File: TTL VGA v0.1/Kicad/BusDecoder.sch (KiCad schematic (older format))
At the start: 12 parts, among them U15 74LS74, U16 74LS32, U17 74LS10, U18 74LS32, U8 74LS139

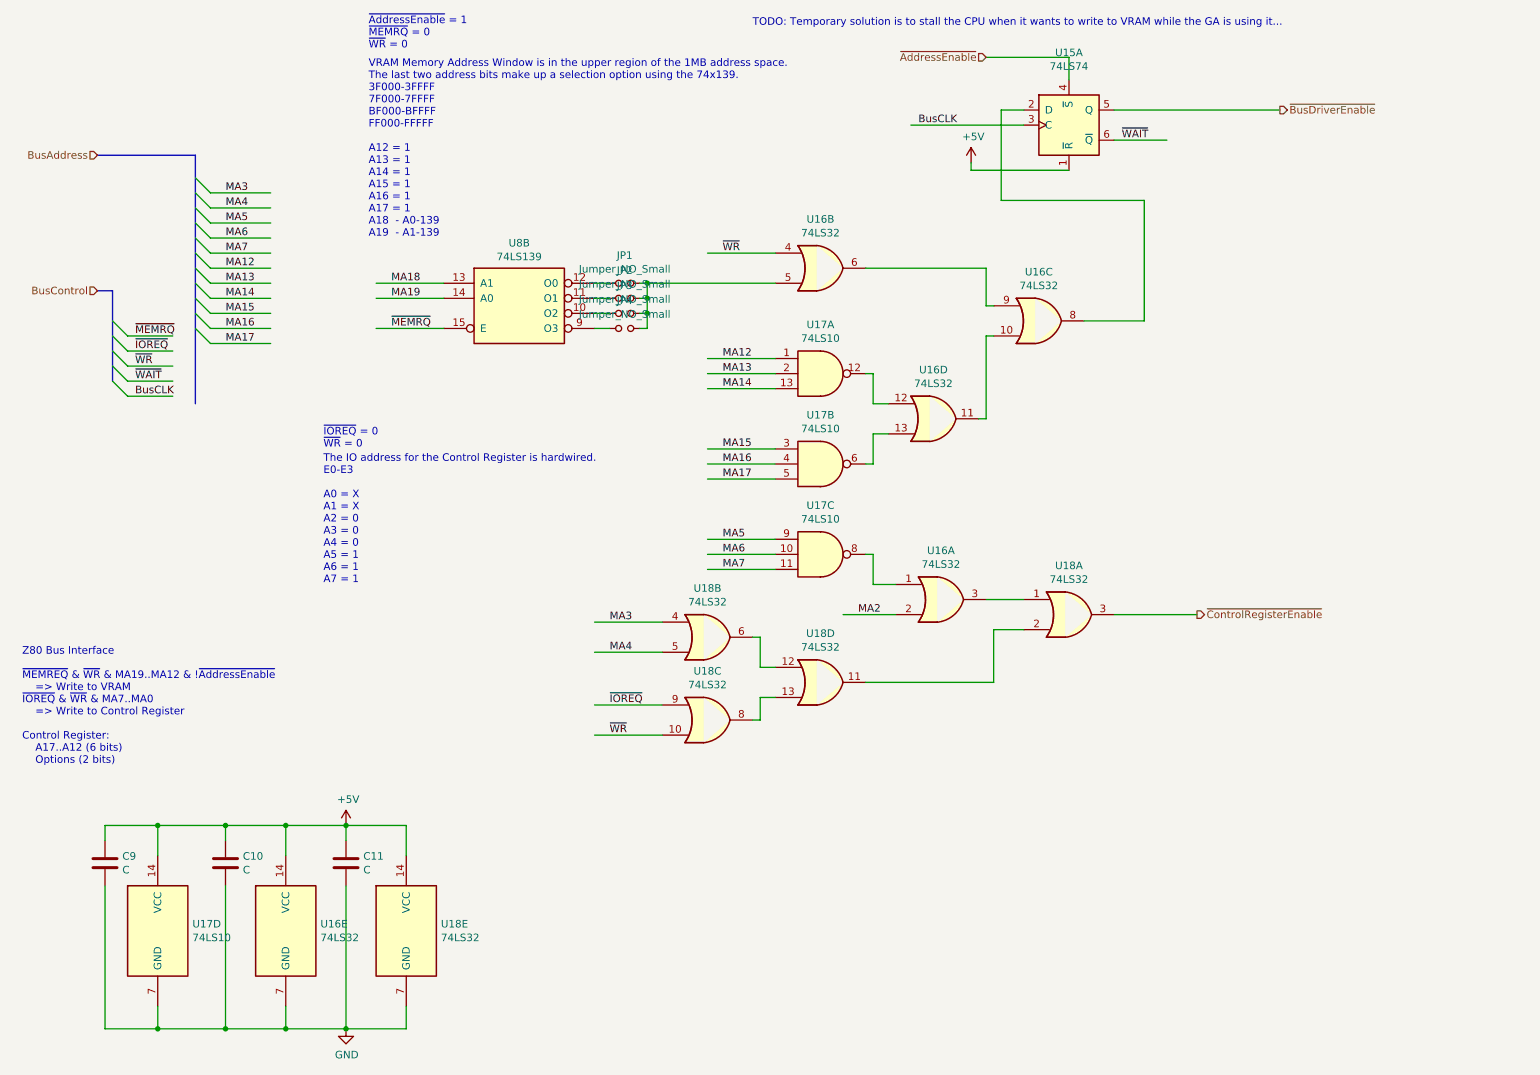
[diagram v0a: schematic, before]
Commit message: vga memory interface
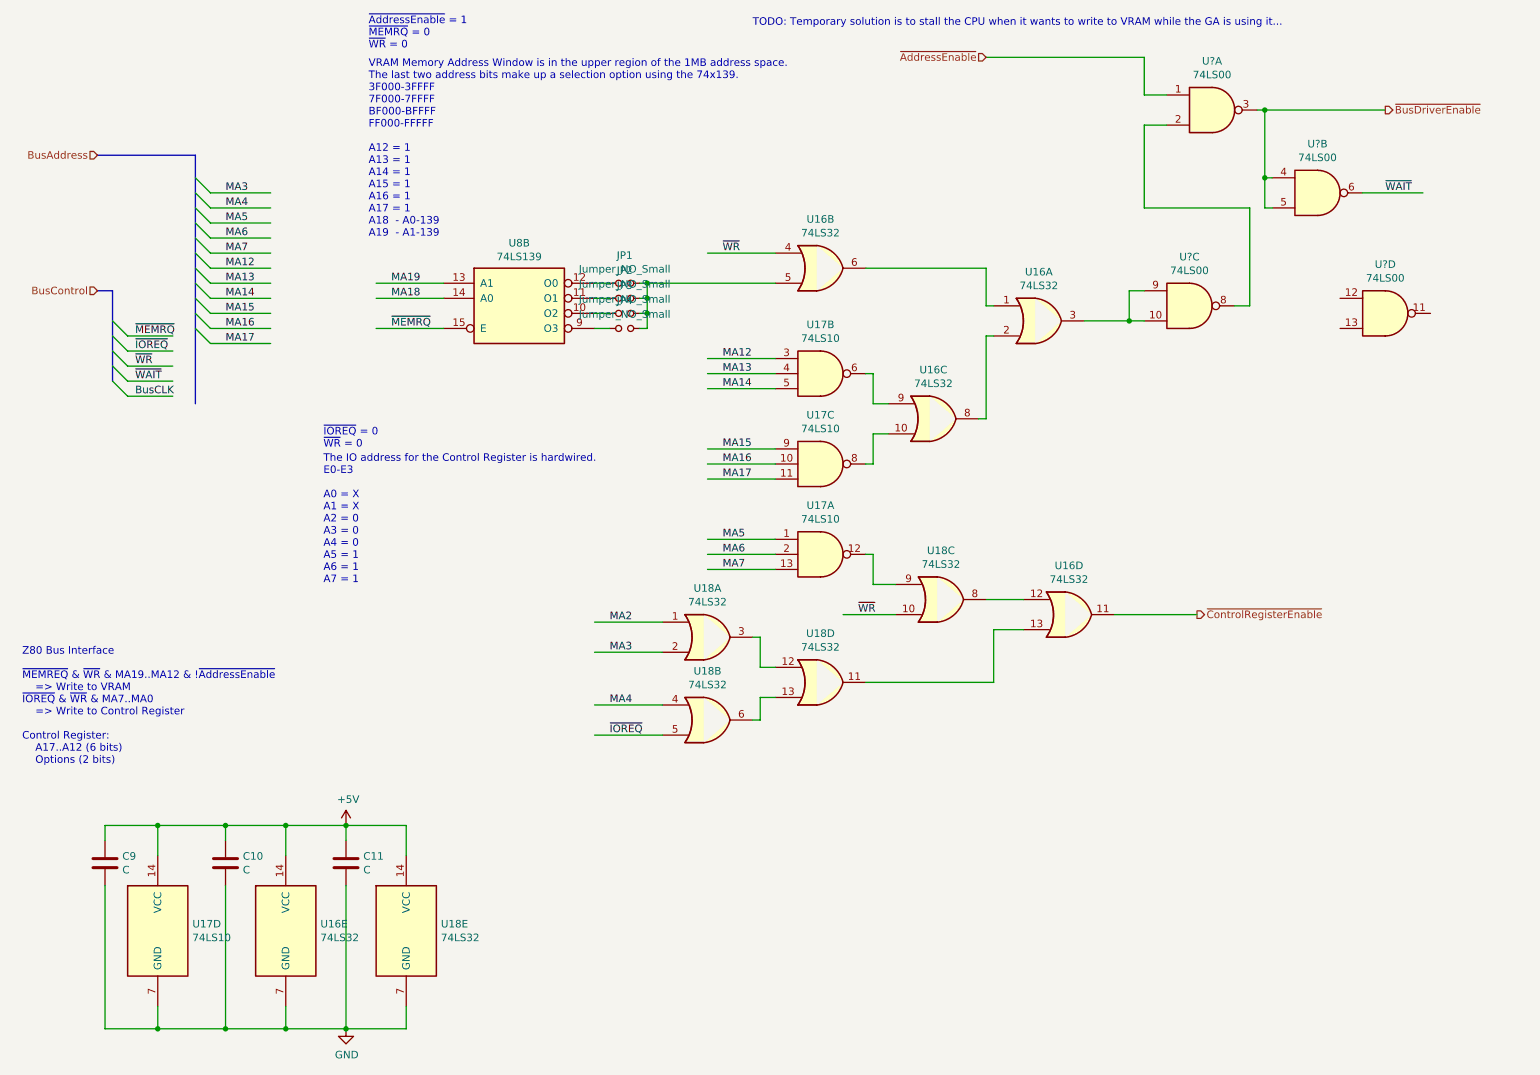
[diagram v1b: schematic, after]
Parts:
- removed U15: 74LS74, symbol 74xx:74LS74
- added U? (x4): 74LS00, symbol 74xx:74LS00
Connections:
- wire segments 106 -> 113
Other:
- moved on the sheet: U16A, U16C, U16D, U17A, U17B, U17C, U18A, U18B, U18C
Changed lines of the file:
@@
 Text HLabel 8650 4550 2    50   Output ~ 0
 ~ControlRegisterEnable
-Text HLabel 9200 1200 2    50   Output ~ 0
+Text HLabel 9900 1200 2    50   Output ~ 0
 ~BusDriverEnable
 Text HLabel 7250 850  0    50   Input ~ 0
@@
 L 74xx:74LS10 U17
 U 1 1 5E729378
+P 6150 4150
+F 0 "U17" H 6150 4475 50  0000 C CNN
+F 1 "74LS10" H 6150 4384 50  0000 C CNN
+F 2 "" H 6150 4150 50  0001 C CNN
+F 3 "http://www.ti.com/lit/gpn/sn74LS10" H 6150 4150 50  0001 C CNN
+	1    6150 4150
+	1    0    0    -1
+$EndComp
+$Comp
+L 74xx:74LS10 U17
+U 2 1 5E7295F8
 P 6150 2950
 F 0 "U17" H 6150 3275 50  0000 C CNN
@@
 F 2 "" H 6150 2950 50  0001 C CNN
 F 3 "http://www.ti.com/lit/gpn/sn74LS10" H 6150 2950 50  0001 C CNN
-	1    6150 2950
+	2    6150 2950
 	1    0    0    -1
 $EndComp
 $Comp
 L 74xx:74LS10 U17
-U 2 1 5E7295F8
+U 3 1 5E72A784
 P 6150 3550
 F 0 "U17" H 6150 3875 50  0000 C CNN
@@
 F 2 "" H 6150 3550 50  0001 C CNN
 F 3 "http://www.ti.com/lit/gpn/sn74LS10" H 6150 3550 50  0001 C CNN
-	2    6150 3550
-	1    0    0    -1
-$EndComp
-$Comp
-L 74xx:74LS10 U17
-U 3 1 5E72A784
-P 6150 4150
-F 0 "U17" H 6150 4475 50  0000 C CNN
-F 1 "74LS10" H 6150 4384 50  0000 C CNN
-F 2 "" H 6150 4150 50  0001 C CNN
-F 3 "http://www.ti.com/lit/gpn/sn74LS10" H 6150 4150 50  0001 C CNN
-	3    6150 4150
+	3    6150 3550
 	1    0    0    -1
 $EndComp
@@
 L 74xx:74LS32 U16
 U 1 1 5E72DE74
-P 6950 4450
-F 0 "U16" H 6950 4775 50  0000 C CNN
-F 1 "74LS32" H 6950 4684 50  0000 C CNN
-F 2 "" H 6950 4450 50  0001 C CNN
-F 3 "http://www.ti.com/lit/gpn/sn74LS32" H 6950 4450 50  0001 C CNN
-	1    6950 4450
+P 7600 2600
+F 0 "U16" H 7600 2925 50  0000 C CNN
+F 1 "74LS32" H 7600 2834 50  0000 C CNN
+F 2 "" H 7600 2600 50  0001 C CNN
+F 3 "http://www.ti.com/lit/gpn/sn74LS32" H 7600 2600 50  0001 C CNN
+	1    7600 2600
 	1    0    0    -1
 $EndComp
@@
 L 74xx:74LS32 U16
 U 3 1 5E72F764
-P 7600 2600
-F 0 "U16" H 7600 2925 50  0000 C CNN
-F 1 "74LS32" H 7600 2834 50  0000 C CNN
-F 2 "" H 7600 2600 50  0001 C CNN
-F 3 "http://www.ti.com/lit/gpn/sn74LS32" H 7600 2600 50  0001 C CNN
-	3    7600 2600
-	1    0    0    -1
-$EndComp
-$Comp
-L 74xx:74LS32 U16
-U 4 1 5E730954
 P 6900 3250
 F 0 "U16" H 6900 3575 50  0000 C CNN
@@
 F 2 "" H 6900 3250 50  0001 C CNN
 F 3 "http://www.ti.com/lit/gpn/sn74LS32" H 6900 3250 50  0001 C CNN
-	4    6900 3250
+	3    6900 3250
+	1    0    0    -1
+$EndComp
+$Comp
+L 74xx:74LS32 U16
+U 4 1 5E730954
+P 7800 4550
+F 0 "U16" H 7800 4875 50  0000 C CNN
+F 1 "74LS32" H 7800 4784 50  0000 C CNN
+F 2 "" H 7800 4550 50  0001 C CNN
+F 3 "http://www.ti.com/lit/gpn/sn74LS32" H 7800 4550 50  0001 C CNN
+	4    7800 4550
 	1    0    0    -1
 $EndComp
@@
 Wire Wire Line
 	3650 2650 3200 2650
+Text Label 3300 2450 0    50   ~ 0
+MA18
 Text Label 3300 2350 0    50   ~ 0
-MA18
-Text Label 3300 2450 0    50   ~ 0
 MA19
 Text Label 3300 2650 0    50   ~ 0
@@
 	7250 3250 7200 3250
 Wire Wire Line
-	7900 2600 8300 2600
-Wire Wire Line
-	8300 2600 8300 1800
+	7900 2600 8200 2600
 Wire Wire Line
 	5850 4250 5400 4250
@@
 L 74xx:74LS32 U18
 U 1 1 5E74F207
-P 7800 4550
-F 0 "U18" H 7800 4875 50  0000 C CNN
-F 1 "74LS32" H 7800 4784 50  0000 C CNN
-F 2 "" H 7800 4550 50  0001 C CNN
-F 3 "http://www.ti.com/lit/gpn/sn74LS32" H 7800 4550 50  0001 C CNN
-	1    7800 4550
-	1    0    0    -1
-$EndComp
-$Comp
-L 74xx:74LS32 U18
-U 2 1 5E751B18
 P 5400 4700
 F 0 "U18" H 5400 5025 50  0000 C CNN
@@
 F 2 "" H 5400 4700 50  0001 C CNN
 F 3 "http://www.ti.com/lit/gpn/sn74LS32" H 5400 4700 50  0001 C CNN
-	2    5400 4700
+	1    5400 4700
+	1    0    0    -1
+$EndComp
+$Comp
+L 74xx:74LS32 U18
+U 2 1 5E751B18
+P 5400 5250
+F 0 "U18" H 5400 5575 50  0000 C CNN
+F 1 "74LS32" H 5400 5484 50  0000 C CNN
+F 2 "" H 5400 5250 50  0001 C CNN
+F 3 "http://www.ti.com/lit/gpn/sn74LS32" H 5400 5250 50  0001 C CNN
+	2    5400 5250
 	1    0    0    -1
 $EndComp
@@
 L 74xx:74LS32 U18
 U 3 1 5E7560E1
-P 5400 5250
-F 0 "U18" H 5400 5575 50  0000 C CNN
-F 1 "74LS32" H 5400 5484 50  0000 C CNN
-F 2 "" H 5400 5250 50  0001 C CNN
-F 3 "http://www.ti.com/lit/gpn/sn74LS32" H 5400 5250 50  0001 C CNN
-	3    5400 5250
+P 6950 4450
+F 0 "U18" H 6950 4775 50  0000 C CNN
+F 1 "74LS32" H 6950 4684 50  0000 C CNN
+F 2 "" H 6950 4450 50  0001 C CNN
+F 3 "http://www.ti.com/lit/gpn/sn74LS32" H 6950 4450 50  0001 C CNN
+	3    6950 4450
 	1    0    0    -1
 $EndComp
@@
 Wire Wire Line
 	4650 5350 5100 5350
-Text Label 4750 4600 0    50   ~ 0
+Text Label 4750 4800 0    50   ~ 0
 MA3
-Text Label 4750 4800 0    50   ~ 0
+Text Label 4750 5150 0    50   ~ 0
 MA4
-Text Label 4750 5150 0    50   ~ 0
+Text Label 4750 5350 0    50   ~ 0
 ~IOREQ
-Text Label 4750 5350 0    50   ~ 0
+Text Label 6400 4550 0    50   ~ 0
 ~WR
 Wire Wire Line
@@
 Wire Wire Line
 	1550 3000 1850 3000
-$Comp
-L 74xx:74LS74 U15
-U 1 1 5E8D5830
-P 7800 1300
-F 0 "U15" H 7800 1781 50  0000 C CNN
-F 1 "74LS74" H 7800 1690 50  0000 C CNN
-F 2 "" H 7800 1300 50  0001 C CNN
-F 3 "74xx/74hc_hct74.pdf" H 7800 1300 50  0001 C CNN
-	1    7800 1300
-	1    0    0    -1
-$EndComp
-Wire Wire Line
-	7250 850  7800 850
-Wire Wire Line
-	7800 850  7800 1000
-Wire Wire Line
-	8300 1800 7350 1800
-Wire Wire Line
-	7350 1800 7350 1200
-Wire Wire Line
-	7350 1200 7500 1200
 Wire Wire Line
 	6450 2250 7250 2250
 Wire Wire Line
 	7250 2250 7250 2500
-Wire Wire Line
-	7500 1300 6750 1300
-Text Label 6800 1300 0    50   ~ 0
-BusCLK
 Entry Wire Line
 	1450 3000 1550 3100
@@
 Text Label 1600 3100 0    50   ~ 0
 BusCLK
-Wire Wire Line
-	8100 1400 8450 1400
-Text Label 8150 1400 0    50   ~ 0
+Text Label 9900 1750 0    50   ~ 0
 ~WAIT
-Wire Wire Line
-	7800 1600 7150 1600
-Wire Wire Line
-	7150 1600 7150 1550
-$Comp
-L power:+5V #PWR034
-U 1 1 5E906D91
-P 7150 1550
-F 0 "#PWR034" H 7150 1400 50  0001 C CNN
-F 1 "+5V" H 7165 1723 50  0000 C CNN
-F 2 "" H 7150 1550 50  0001 C CNN
-F 3 "" H 7150 1550 50  0001 C CNN
-	1    7150 1550
-	1    0    0    -1
-$EndComp
 Text Notes 5700 650  0    50   ~ 0
 TODO: Temporary solution is to stall the CPU when it wants to write to VRAM while the GA is using it...
 Wire Wire Line
-	8100 1200 9200 1200
-Wire Wire Line
 	6300 4550 6650 4550
 Wire Wire Line
@@
 Wire Wire Line
 	7300 4650 7300 5000
-Text Label 6400 4550 0    50   ~ 0
+Text Label 4750 4600 0    50   ~ 0
 MA2
 Wire Wire Line
 	8100 4550 8650 4550
+$Comp
+L 74xx:74LS00 U?
+U 1 1 5E61D130
+P 8750 1200
+F 0 "U?" H 8750 1525 50  0000 C CNN
+F 1 "74LS00" H 8750 1434 50  0000 C CNN
+F 2 "" H 8750 1200 50  0001 C CNN
+F 3 "http://www.ti.com/lit/gpn/sn74ls00" H 8750 1200 50  0001 C CNN
+	1    8750 1200
+	1    0    0    -1
+$EndComp
+$Comp
+L 74xx:74LS00 U?
+U 2 1 5E628EB2
+P 9450 1750
+F 0 "U?" H 9450 2075 50  0000 C CNN
+F 1 "74LS00" H 9450 1984 50  0000 C CNN
+F 2 "" H 9450 1750 50  0001 C CNN
+F 3 "http://www.ti.com/lit/gpn/sn74ls00" H 9450 1750 50  0001 C CNN
+	2    9450 1750
+	1    0    0    -1
+$EndComp
+$Comp
+L 74xx:74LS00 U?
+U 3 1 5E62BDF3
+P 8600 2500
+F 0 "U?" H 8600 2825 50  0000 C CNN
+F 1 "74LS00" H 8600 2734 50  0000 C CNN
+F 2 "" H 8600 2500 50  0001 C CNN
+F 3 "http://www.ti.com/lit/gpn/sn74ls00" H 8600 2500 50  0001 C CNN
+	3    8600 2500
+	1    0    0    -1
+$EndComp
+$Comp
+L 74xx:74LS00 U?
+U 4 1 5E62EF03
+P 9900 2550
+F 0 "U?" H 9900 2875 50  0000 C CNN
+F 1 "74LS00" H 9900 2784 50  0000 C CNN
+F 2 "" H 9900 2550 50  0001 C CNN
+F 3 "http://www.ti.com/lit/gpn/sn74ls00" H 9900 2550 50  0001 C CNN
+	4    9900 2550
+	1    0    0    -1
+$EndComp
+Wire Wire Line
+	8300 2400 8200 2400
+Wire Wire Line
+	8200 2400 8200 2600
+Connection ~ 8200 2600
+Wire Wire Line
+	8200 2600 8300 2600
+Wire Wire Line
+	8900 2500 9000 2500
+Wire Wire Line
+	9000 2500 9000 1850
+Wire Wire Line
+	9000 1850 8300 1850
+Wire Wire Line
+	8300 1850 8300 1300
+Wire Wire Line
+	8300 1300 8450 1300
+Wire Wire Line
+	8300 850  8300 1100
+Wire Wire Line
+	8300 1100 8450 1100
+Wire Wire Line
+	9050 1200 9100 1200
+Wire Wire Line
+	9750 1750 10150 1750
+Wire Wire Line
+	7250 850  8300 850
+Wire Wire Line
+	9100 1200 9100 1650
+Wire Wire Line
+	9100 1850 9150 1850
+Connection ~ 9100 1200
+Wire Wire Line
+	9100 1200 9900 1200
+Wire Wire Line
+	9150 1650 9100 1650
+Connection ~ 9100 1650
+Wire Wire Line
+	9100 1650 9100 1850
 Wire Bus Line
 	1450 2400 1450 3000

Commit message: vga test code
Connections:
- wire segments 113 -> 118
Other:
- moved on the sheet: U?D
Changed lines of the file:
@@
 	1    0    0    -1
 $EndComp
-Text HLabel 8650 4550 2    50   Output ~ 0
+Text HLabel 9300 4550 2    50   Output ~ 0
 ~ControlRegisterEnable
 Text HLabel 9900 1200 2    50   Output ~ 0
@@
 Text Label 4750 4600 0    50   ~ 0
 MA2
-Wire Wire Line
-	8100 4550 8650 4550
 $Comp
 L 74xx:74LS00 U?
@@
 L 74xx:74LS00 U?
 U 4 1 5E62EF03
-P 9900 2550
-F 0 "U?" H 9900 2875 50  0000 C CNN
-F 1 "74LS00" H 9900 2784 50  0000 C CNN
-F 2 "" H 9900 2550 50  0001 C CNN
-F 3 "http://www.ti.com/lit/gpn/sn74ls00" H 9900 2550 50  0001 C CNN
-	4    9900 2550
+P 8650 4550
+F 0 "U?" H 8650 4875 50  0000 C CNN
+F 1 "74LS00" H 8650 4784 50  0000 C CNN
+F 2 "" H 8650 4550 50  0001 C CNN
+F 3 "http://www.ti.com/lit/gpn/sn74ls00" H 8650 4550 50  0001 C CNN
+	4    8650 4550
 	1    0    0    -1
 $EndComp
@@
 Wire Wire Line
 	9100 1650 9100 1850
+Wire Wire Line
+	8100 4550 8250 4550
+Wire Wire Line
+	8250 4550 8250 4450
+Wire Wire Line
+	8250 4450 8350 4450
+Wire Wire Line
+	8350 4650 8250 4650
+Wire Wire Line
+	8250 4650 8250 4550
+Connection ~ 8250 4550
+Wire Wire Line
+	8950 4550 9300 4550
 Wire Bus Line
 	1450 2400 1450 3000

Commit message: More VGA work
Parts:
- removed JP1, JP2, JP3, JP4: Jumper_NO_Small, symbol Device:Jumper_NO_Small
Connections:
- wire segments 118 -> 107
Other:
- note added: "I dont think this is correct"
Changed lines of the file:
@@
 Text Label 3300 2650 0    50   ~ 0
 ~MEMRQ
-$Comp
-L Device:Jumper_NO_Small JP1
-U 1 1 5E73F012
-P 4850 2350
-F 0 "JP1" H 4850 2535 50  0000 C CNN
-F 1 "Jumper_NO_Small" H 4850 2444 50  0000 C CNN
-F 2 "" H 4850 2350 50  0001 C CNN
-F 3 "~" H 4850 2350 50  0001 C CNN
-	1    4850 2350
-	1    0    0    -1
-$EndComp
-$Comp
-L Device:Jumper_NO_Small JP2
-U 1 1 5E73FE6D
-P 4850 2450
-F 0 "JP2" H 4850 2635 50  0000 C CNN
-F 1 "Jumper_NO_Small" H 4850 2544 50  0000 C CNN
-F 2 "" H 4850 2450 50  0001 C CNN
-F 3 "~" H 4850 2450 50  0001 C CNN
-	1    4850 2450
-	1    0    0    -1
-$EndComp
-$Comp
-L Device:Jumper_NO_Small JP3
-U 1 1 5E7405F6
-P 4850 2550
-F 0 "JP3" H 4850 2735 50  0000 C CNN
-F 1 "Jumper_NO_Small" H 4850 2644 50  0000 C CNN
-F 2 "" H 4850 2550 50  0001 C CNN
-F 3 "~" H 4850 2550 50  0001 C CNN
-	1    4850 2550
-	1    0    0    -1
-$EndComp
-$Comp
-L Device:Jumper_NO_Small JP4
-U 1 1 5E740C9C
-P 4850 2650
-F 0 "JP4" H 4850 2835 50  0000 C CNN
-F 1 "Jumper_NO_Small" H 4850 2744 50  0000 C CNN
-F 2 "" H 4850 2650 50  0001 C CNN
-F 3 "~" H 4850 2650 50  0001 C CNN
-	1    4850 2650
-	1    0    0    -1
-$EndComp
-Wire Wire Line
-	4650 2350 4750 2350
-Wire Wire Line
-	4650 2450 4750 2450
-Wire Wire Line
-	4650 2550 4750 2550
-Wire Wire Line
-	4650 2650 4750 2650
-Wire Wire Line
-	4950 2650 5000 2650
-Wire Wire Line
-	5000 2650 5000 2550
-Wire Wire Line
-	5000 2350 4950 2350
-Wire Wire Line
-	4950 2450 5000 2450
-Connection ~ 5000 2450
-Wire Wire Line
-	5000 2450 5000 2350
-Wire Wire Line
-	4950 2550 5000 2550
-Connection ~ 5000 2550
-Wire Wire Line
-	5000 2550 5000 2450
-Wire Wire Line
-	5000 2350 5850 2350
-Connection ~ 5000 2350
 Wire Wire Line
 	7300 2700 7250 2700
@@
 F 3 "http://www.ti.com/lit/gpn/sn74LS32" H 6150 5000 50  0001 C CNN
 	4    6150 5000
-	1    0    0    -1
+	1    0    0    1
 $EndComp
 $Comp
@@
 F 3 "http://www.ti.com/lit/gpn/sn74LS32" H 6950 4450 50  0001 C CNN
 	3    6950 4450
-	1    0    0    -1
+	1    0    0    1
 $EndComp
 $Comp
@@
 Text Label 1600 3100 0    50   ~ 0
 BusCLK
-Text Label 9900 1750 0    50   ~ 0
+Text Label 10250 1750 0    50   ~ 0
 ~WAIT
 Text Notes 5700 650  0    50   ~ 0
@@
 	9050 1200 9100 1200
 Wire Wire Line
-	9750 1750 10150 1750
-Wire Wire Line
 	7250 850  8300 850
 Wire Wire Line
@@
 Wire Wire Line
 	8950 4550 9300 4550
+Wire Wire Line
+	4650 2350 5850 2350
+Text Notes 9400 2000 0    50   ~ 0
+I dont think this is correct
+Wire Wire Line
+	10450 1750 10150 1750
 Wire Bus Line
 	1450 2400 1450 3000
